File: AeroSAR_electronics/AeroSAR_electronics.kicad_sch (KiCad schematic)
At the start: 16 parts, among them J1 USB_B_Micro, J10 Receiver, J11 Rpi, J12 GPS, J2 ESC-1, J3 ESC-2, J4 Servo, J5 Servo, J6 Servo, J7 Servo, J8 Servo, J9 Compass

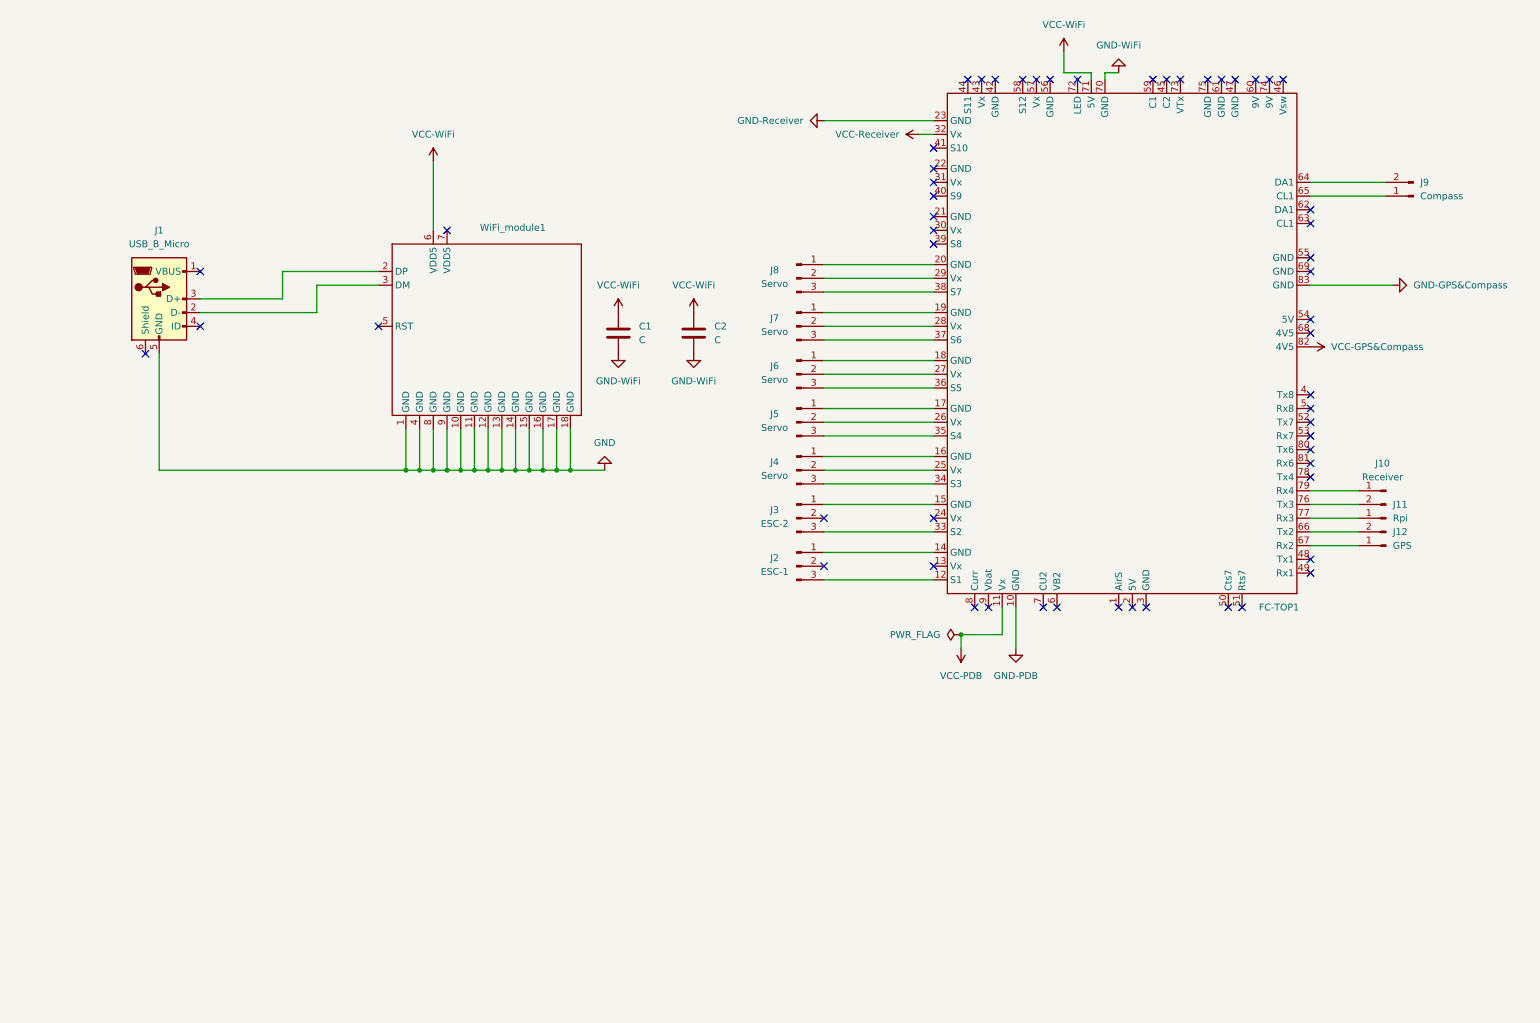
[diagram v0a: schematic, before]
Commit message: Added terminals and reworked USB implementation
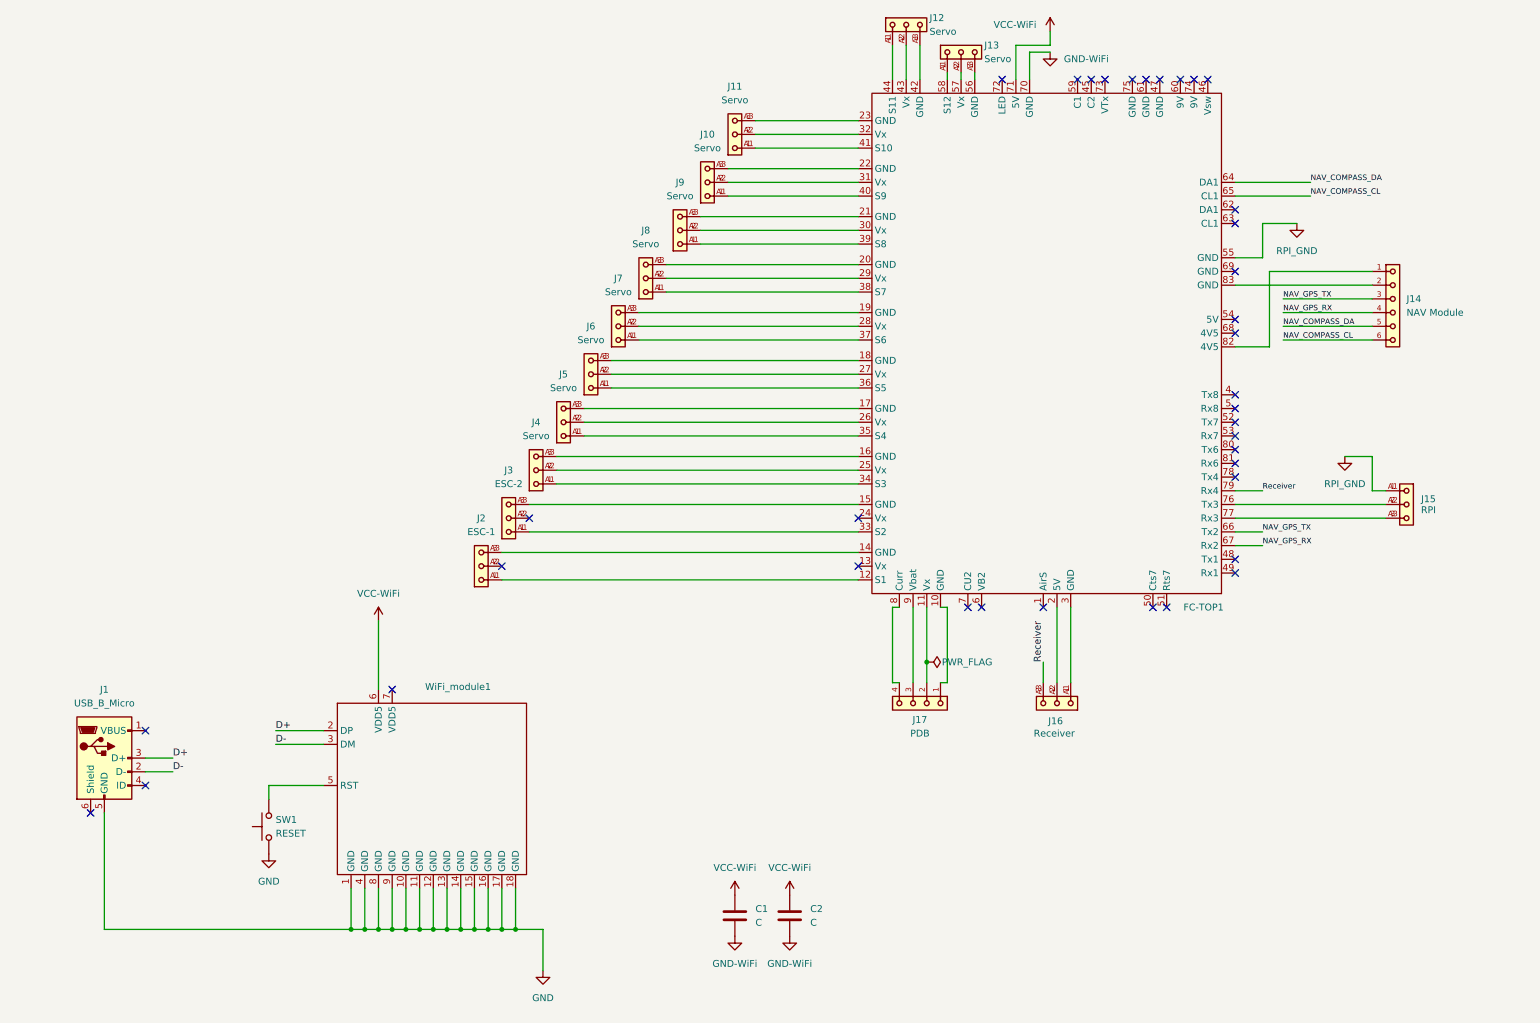
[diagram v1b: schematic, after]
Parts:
- removed J10: Receiver, symbol Connector:Conn_01x01_Pin
- removed J11: Rpi, symbol Connector:Conn_01x02_Pin
- removed J12: GPS, symbol Connector:Conn_01x02_Pin
- removed J2: ESC-1, symbol Connector:Conn_01x03_Pin
- removed J3: ESC-2, symbol Connector:Conn_01x03_Pin
- removed J4, J5, J6, J7, J8: Servo, symbol Connector:Conn_01x03_Pin
- removed J9: Compass, symbol Connector:Conn_01x02_Pin
- added J10, J11, J12, J13, J4, J5, J6, J7, J8, J9: Servo, BL-M8812EU3:691403900003B, symbol Spring_Clip_Terminal:691403900006B_3
- added J14: NAV Module, BL-M8812EU6:691403900006B, symbol Spring_Clip_Terminal:691403900006B
- added J15: RPI, BL-M8812EU3:691403900003B, symbol Spring_Clip_Terminal:691403900006B_3
- added J16: Receiver, BL-M8812EU3:691403900003B, symbol Spring_Clip_Terminal:691403900006B_3
- added J17: PDB, BL-M8812EU4:691403900004B, symbol Spring_Clip_Terminal:691403900004B
- added J2: ESC-1, BL-M8812EU3:691403900003B, symbol Spring_Clip_Terminal:691403900006B_3
- added J3: ESC-2, BL-M8812EU3:691403900003B, symbol Spring_Clip_Terminal:691403900006B_3
- added SW1: RESET, symbol Switch:SW_Push
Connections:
- net GND: now also SW1.1
- net Receiver: now reaches FC-TOP1.79 (Rx4)
- net Receiver: now also J16.3, J16.A3
- net at FC-TOP1.18 (GND): now also J6.3, J6.A3
- net at FC-TOP1.27 (Vx): now also J6.2, J6.A2
- net at FC-TOP1.36 (S5): now also J6.1, J6.A1
- net at FC-TOP1.14 (GND): now also J2.3, J2.A3
- net at FC-TOP1.12 (S1): now also J2.1, J2.A1
- net at FC-TOP1.15 (GND): now also J3.3, J3.A3
- net at FC-TOP1.16 (GND): now also J4.3, J4.A3
- net at FC-TOP1.17 (GND): now also J5.3, J5.A3
- net at FC-TOP1.19 (GND): now also J7.3, J7.A3
- net at FC-TOP1.2 (5V): now also J16.2, J16.A2
- net at FC-TOP1.20 (GND): now also J8.3, J8.A3
- net at FC-TOP1.21 (GND): now also J9.3, J9.A3
- net at FC-TOP1.22 (GND): now also J10.3, J10.A3
- net at FC-TOP1.25 (Vx): now also J4.2, J4.A2
- net at FC-TOP1.26 (Vx): now also J5.2, J5.A2
- net at FC-TOP1.28 (Vx): now also J7.2, J7.A2
- net at FC-TOP1.29 (Vx): now also J8.2, J8.A2
- net at FC-TOP1.3 (GND): now also J16.1, J16.A1
- net at FC-TOP1.30 (Vx): now also J9.2, J9.A2
- net at FC-TOP1.31 (Vx): now also J10.2, J10.A2
- net at FC-TOP1.33 (S2): now also J3.1, J3.A1
- net at FC-TOP1.34 (S3): now also J4.1, J4.A1
- net at FC-TOP1.35 (S4): now also J5.1, J5.A1
- net at FC-TOP1.37 (S6): now also J7.1, J7.A1
- net at FC-TOP1.38 (S7): now also J8.1, J8.A1
- net at FC-TOP1.39 (S8): now also J9.1, J9.A1
- net at FC-TOP1.40 (S9): now also J10.1, J10.A1
- net at FC-TOP1.41 (S10): now also J11.1, J11.A1
- net at FC-TOP1.42 (GND): now also J12.3, J12.A3
- net at FC-TOP1.43 (Vx): now also J12.2, J12.A2
- net at FC-TOP1.44 (S11): now also J12.1, J12.A1
- net RPI_GND: now reaches FC-TOP1.55 (GND)
- net RPI_GND: now also J15.1, J15.A1
- net at FC-TOP1.56 (GND): now also J13.3, J13.A3
- net at FC-TOP1.57 (Vx): now also J13.2, J13.A2
- net at FC-TOP1.58 (S12): now also J13.1, J13.A1
- net NAV_COMPASS_DA: now reaches FC-TOP1.64 (DA1)
- net NAV_COMPASS_DA: now also J14.5, J14.A5
- net NAV_COMPASS_CL: now reaches FC-TOP1.65 (CL1)
- net NAV_COMPASS_CL: now also J14.6, J14.A6
- net NAV_GPS_TX: now reaches FC-TOP1.66 (Tx2)
- net NAV_GPS_TX: now also J14.3, J14.A3
- net NAV_GPS_RX: now reaches FC-TOP1.67 (Rx2)
- net NAV_GPS_RX: now also J14.4, J14.A4
- net at FC-TOP1.76 (Tx3): now also J15.2, J15.A2
- net at FC-TOP1.77 (Rx3): now also J15.3, J15.A3
- net at FC-TOP1.8 (Curr): now also J17.4, J17.A4
- net at FC-TOP1.9 (Vbat): now also J17.3, J17.A3
- net D-: now reaches J1.2 (D-), WiFi_module1.3 (DM)
- net D+: now reaches J1.3 (D+), WiFi_module1.2 (DP)
- net at WiFi_module1.5 (RST): now also SW1.2
- net GND-GPS&Compass: no longer names the net of FC-TOP1.83 (GND)
- net GND-GPS&Compass: now also J14.2, J14.A2
- net GND-PDB: no longer names the net of FC-TOP1.10 (GND)
- net GND-PDB: now also J17.1, J17.A1
- net GND-Receiver: no longer names the net of FC-TOP1.23 (GND)
- net GND-Receiver: now also J11.3, J11.A3
- net VCC-GPS&Compass: no longer names the net of FC-TOP1.82 (4V5)
- net VCC-GPS&Compass: now also J14.1, J14.A1
- net VCC-PDB: no longer names the net of FC-TOP1.11 (Vx)
- net VCC-PDB: now also J17.2, J17.A2
- net VCC-Receiver: no longer names the net of FC-TOP1.32 (Vx)
- net VCC-Receiver: now also J11.2, J11.A2
- new net: J3.2, J3.A2
- new net: J2.2, J2.A2
- no-connect marks 56 -> 37
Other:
- moved on the sheet: C1, C2, FC-TOP1, J1, WiFi_module1

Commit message: Wired terminal, added mounting holes and copper zones with via stitching
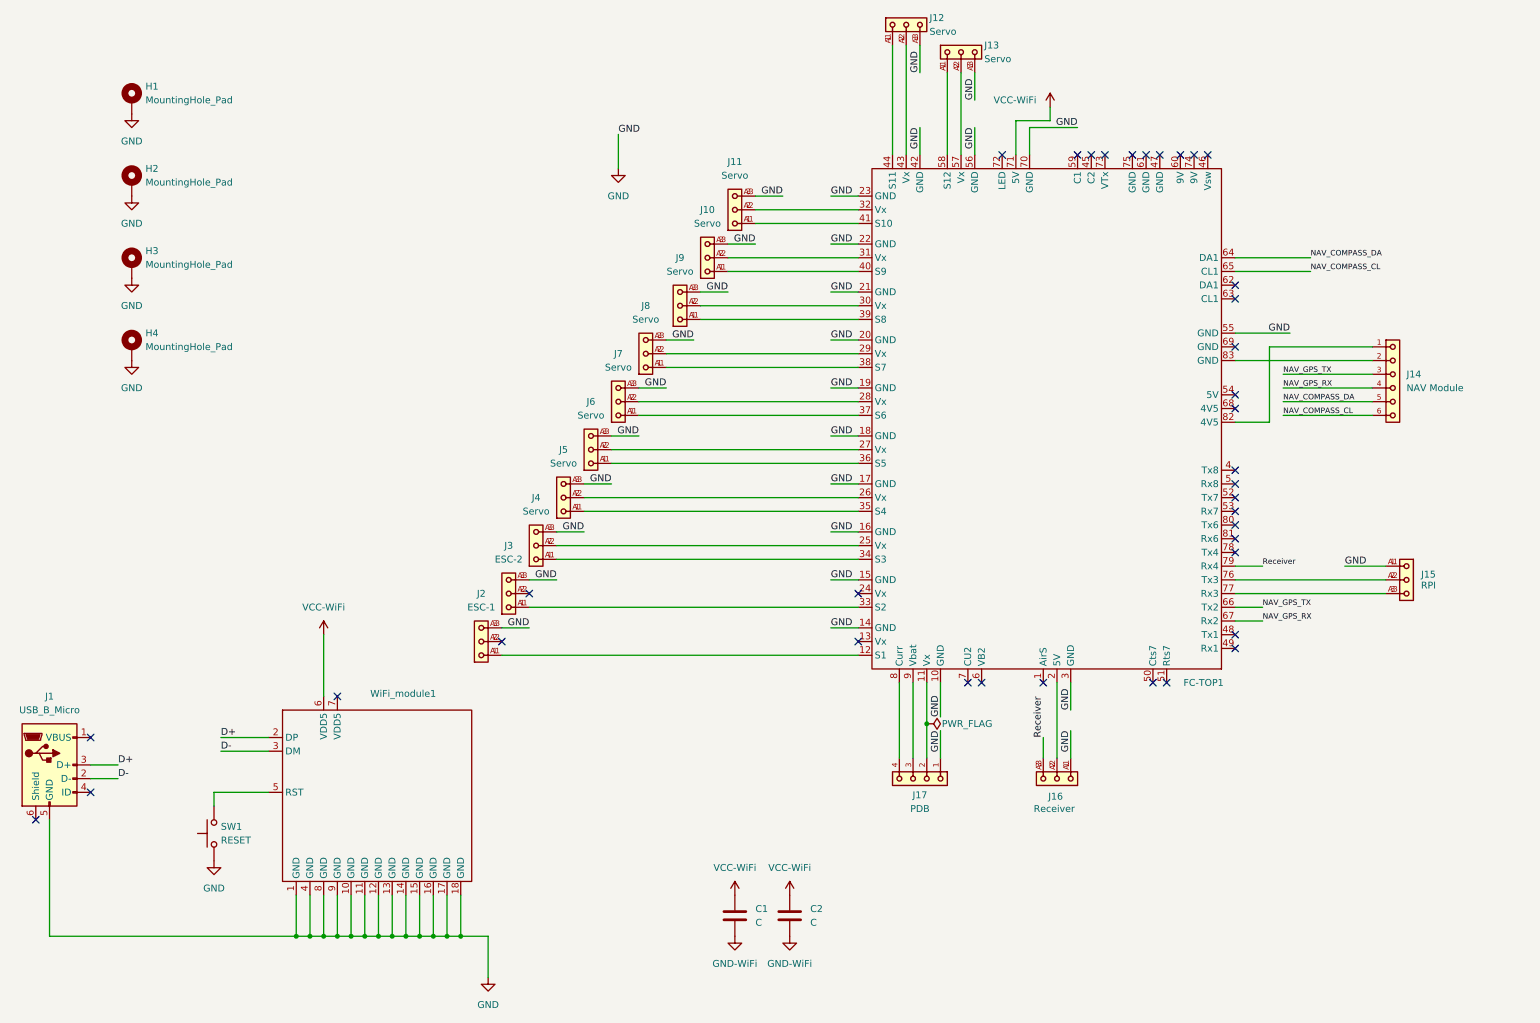
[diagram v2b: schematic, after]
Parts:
- added H1, H2, H3, H4: MountingHole_Pad, MountingHole:MountingHole_3.2mm_M3_Pad, symbol Mechanical:MountingHole_Pad
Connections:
- net RPI_GND is gone; now on net GND: FC-TOP1.55 (GND), J15.1, J15.A1
- net GND: now also FC-TOP1.10 (GND), FC-TOP1.14 (GND), FC-TOP1.15 (GND), FC-TOP1.16 (GND), FC-TOP1.17 (GND), FC-TOP1.18 (GND), FC-TOP1.19 (GND), FC-TOP1.20 (GND), FC-TOP1.21 (GND), FC-TOP1.22 (GND), FC-TOP1.23 (GND), FC-TOP1.3 (GND), FC-TOP1.42 (GND), FC-TOP1.56 (GND), FC-TOP1.70 (GND), J10.3, J10.A3, J11.3, J11.A3, J12.3, J12.A3, J13.3, J13.A3, J16.1, J16.A1, J17.1, J17.A1, J2.3, J2.A3, J3.3, J3.A3, J4.3, J4.A3, J5.3, J5.A3, J6.3, J6.A3, J7.3, J7.A3, J8.3, J8.A3, J9.3, J9.A3, H1.1, H2.1, H3.1, H4.1
- net GND-WiFi: no longer FC-TOP1.70 (GND)
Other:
- moved on the sheet: FC-TOP1, J1, J10, J11, J14, J15, J16, J17, J2, J3, J4, J5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
